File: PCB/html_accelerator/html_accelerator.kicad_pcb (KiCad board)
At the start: 4 copper layers, 129.3 x 104.4 mm, 170 parts, among them J1 Bus_PCI_Express_x16, J2 PCIexpress_bracket, U1 MCS9990, U10 AU6438BS, U11 EMMC_4G, U12 MCS9990, U2 AP1513, U3 CAT24C256YI-GT3, U4 AU6438BS, U5 EMMC_4G, U6 EMMC_4G, U7 EMMC_4G, U8 AU6438BS, U9 AU6438BS, Y1 12MHz, Y2 12MHz, Y3 12MHz, Y4 12MHz, Y5 12MHz

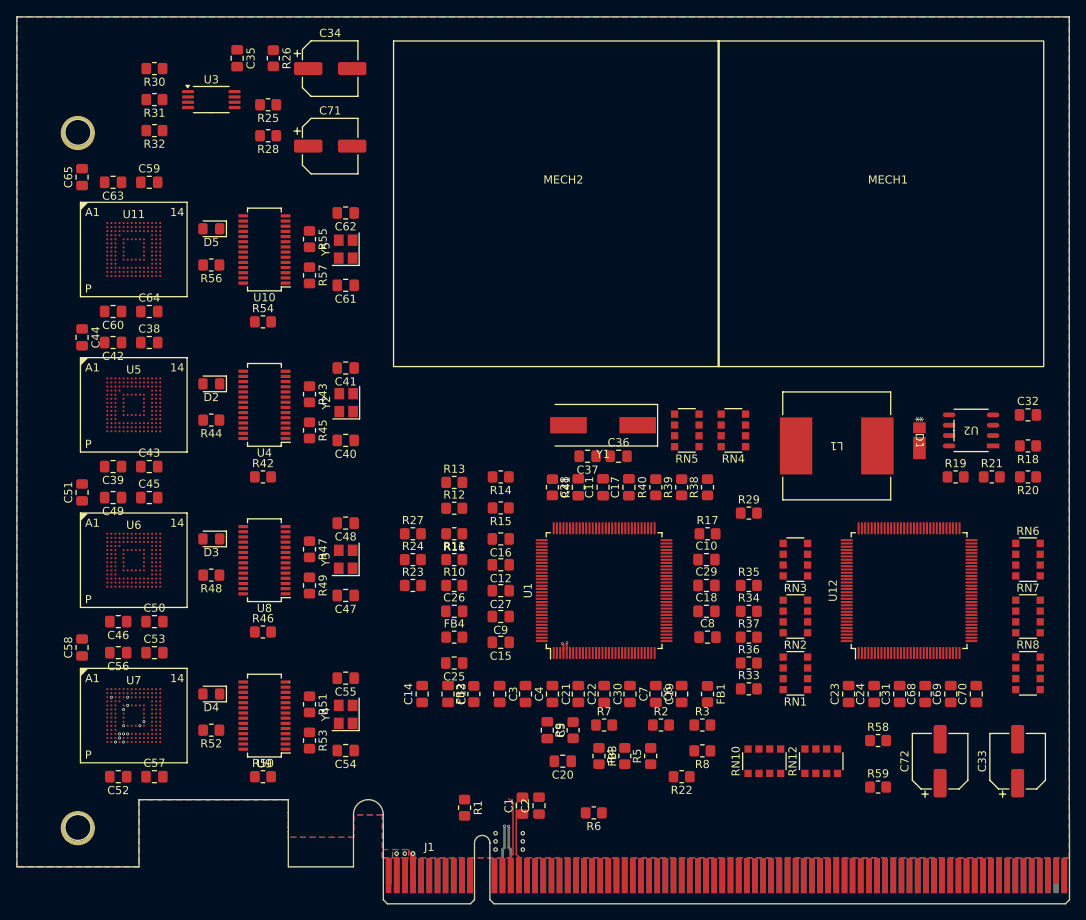
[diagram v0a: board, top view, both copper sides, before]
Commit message: PCIE routing+Shield
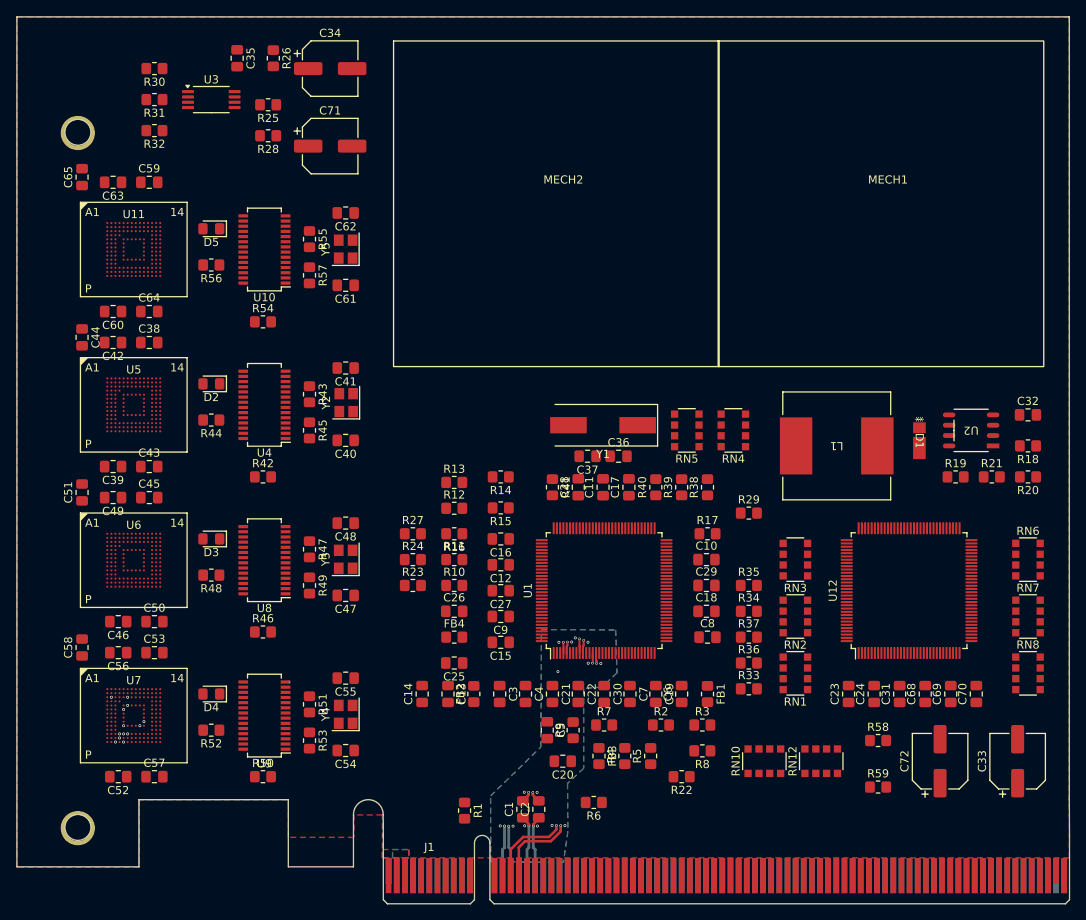
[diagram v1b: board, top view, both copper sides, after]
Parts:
- moved R6 1.28 mm to (185.2, 147.1)
- moved C1 0.45 mm to (176.5, 148.0)
- moved C2 0.45 mm to (178.4, 148.0)
- moved R1 0.35 mm to (169.3, 148.1)
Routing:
- net /PCIE_Slot/85_PCIE_RX_N: track 9.67 -> 42.7 mm, vias 0 -> 2
- net /PCIE_Slot/85_PCIE_RX_P: track 9.69 -> 41.5 mm, vias 0 -> 2
- net /PCIE_Slot/85_PCIE_TXC_P: track 0.00 -> 23.3 mm, vias 0 -> 2
- net /PCIE_Slot/85_PCIE_TXC_N: track 0.00 -> 23.2 mm, vias 0 -> 2
- net /PCIE_Slot/85_PCIE_TX_P: track 0.00 -> 7.55 mm, vias 0 -> 1
- net /PCIE_Slot/85_PCIE_TX_N: track 0.00 -> 7.46 mm, vias 0 -> 1
- net GND: track 2.62 -> 0.00 mm, vias 7 -> 15
- net +12V: track 2.62 -> 0.00 mm, vias 2 -> 0
- net /PCIE_Slot/85_PCIE_CLK_P: track 34.5 -> 36.1 mm
- net /PCIE_Slot/85_PCIE_CLK_N: track 33.2 -> 34.4 mm
- removed copper zone on In2.Cu, net GND

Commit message: trace routing
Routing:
- net +12V: track 0.00 -> 101.1 mm, vias 0 -> 2
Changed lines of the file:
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@@
   )
   (target plus (at 159.467 159.533) (size 5) (width 0.05) (layer "Edge.Cuts"))
+  (segment (start 226.555 146.205) (end 227.755 145.005) (width 1) (layer "F.Cu") (net 4))
+  (segment (start 226.555 149.945) (end 226.555 146.205) (width 1) (layer "F.Cu") (net 4))
+  (segment (start 168.825 144.475) (end 187.095 144.475) (width 1) (layer "F.Cu") (net 4))
+  (segment (start 187.095 144.475) (end 192.565 149.945) (width 1) (layer "F.Cu") (net 4))
+  (segment (start 192.565 149.945) (end 226.555 149.945) (width 1) (layer "F.Cu") (net 4))
+  (segment (start 226.555 149.945) (end 232.525 149.945) (width 1) (layer "F.Cu") (net 4))
+  (segment (start 160.983 153.437) (end 161.025 153.395) (width 0.2) (layer "F.Cu") (net 4))
+  (segment (start 160.983 156.121) (end 160.983 153.437) (width 0.2) (layer "F.Cu") (net 4))
+  (segment (start 237.255 145.215) (end 237.255 144.925) (width 1) (layer "F.Cu") (net 4))
+  (segment (start 161.025 152.275) (end 161.025 152.145) (width 0.2) (layer "F.Cu") (net 4))
+  (segment (start 162.005 153.405) (end 162.005 156.115) (width 0.2) (layer "F.Cu") (net 4))
+  (segment (start 161.025 152.275) (end 168.825 144.475) (width 1) (layer "F.Cu") (net 4))
+  (segment (start 161.025 153.395) (end 161.025 152.275) (width 1) (layer "F.Cu") (net 4))
+  (segment (start 232.525 149.945) (end 237.255 145.215) (width 1) (layer "F.Cu") (net 4))
+  (via (at 161.025 153.395) (size 0.35) (drill 0.2) (layers "F.Cu" "B.Cu") (net 4))
+  (via (at 162.005 153.405) (size 0.35) (drill 0.2) (layers "F.Cu" "B.Cu") (net 4))
+  (segment (start 162.005 153.405) (end 162.005 155.475) (width 0.2) (layer "B.Cu") (net 4))
+  (segment (start 161.025 153.395) (end 161.995 153.395) (width 0.2) (layer "B.Cu") (net 4))
+  (segment (start 161.025 153.395) (end 161.025 155.305) (width 0.2) (layer "B.Cu") (net 4))
+  (segment (start 161.995 153.395) (end 162.005 153.405) (width 0.2) (layer "B.Cu") (net 4))
   (via (at 184.506401 130.015583) (size 0.35) (drill 0.2) (layers "F.Cu" "B.Cu") (free) (net 104))
   (via (at 176.651527 145.863238) (size 0.35) (drill 0.2) (layers "F.Cu" "B.Cu") (free) (net 104))
@@
       )
     )
+  )
+  (zone locked (net 104) (net_name "GND") (layer "B.Cu") (name "PCIE_SHIELD2") (hatch edge 0.5)
+    (priority 3)
+    (connect_pads (clearance 0))
+    (min_thickness 0.25) (filled_areas_thickness no)
+    (fill yes (thermal_gap 0.5) (thermal_bridge_width 0.5))
+    (polygon
+      (pts
+        (xy 181.455 154.485)
+        (xy 172.535 154.395)
+        (xy 172.525 149.555)
+        (xy 182.035 149.555)
+        (xy 182.015 150.655)
+      )
+    )

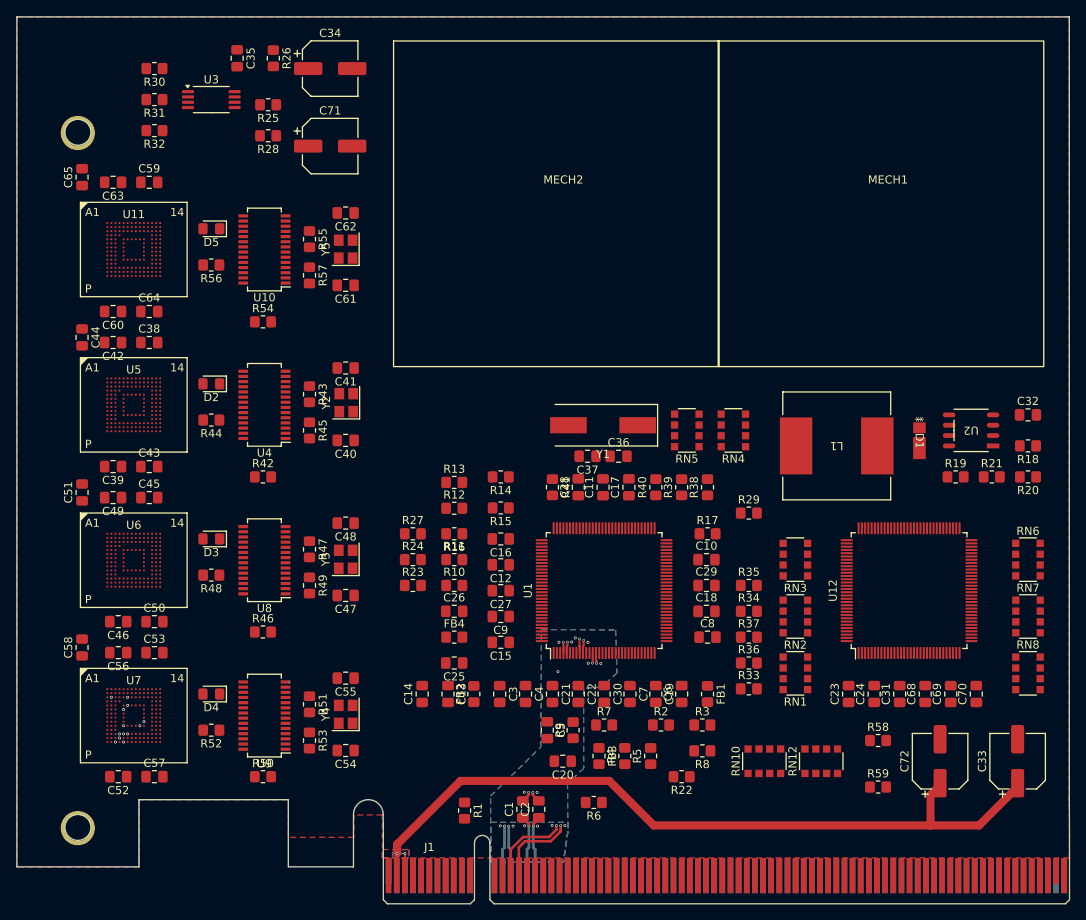
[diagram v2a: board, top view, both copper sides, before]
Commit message: Impedance control routing 90 and 85 ohm
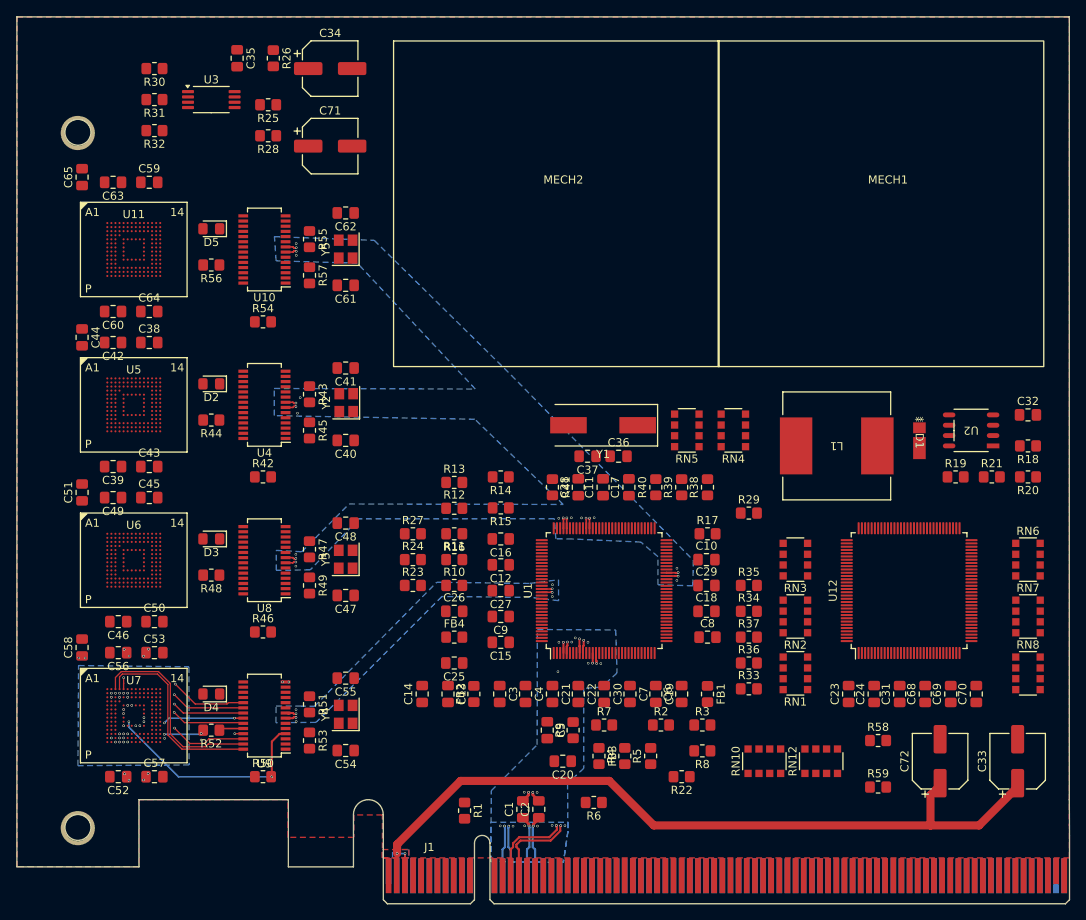
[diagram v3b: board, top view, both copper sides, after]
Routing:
- net 90_USB3_D_N: track 0.00 -> 69.0 mm, vias 0 -> 2
- net 90_USB3_D_P: track 0.00 -> 67.5 mm, vias 0 -> 2
- net 90_USB0_D_N: track 0.00 -> 45.5 mm, vias 0 -> 2
- net 90_USB0_D_P: track 0.00 -> 44.8 mm, vias 0 -> 2
- net 90_USB2_D_N: track 0.00 -> 41.2 mm, vias 0 -> 2
- net 90_USB2_D_P: track 0.00 -> 40.9 mm, vias 0 -> 2
- net 90_USB1_D_N: track 0.00 -> 39.1 mm, vias 0 -> 2
- net 90_USB1_D_P: track 0.00 -> 38.4 mm, vias 0 -> 2
- net Net-(U7A-RST_N): track 0.00 -> 28.1 mm, vias 1 -> 3
- net /eMMC3/DATA_0: track 0.00 -> 25.0 mm
- net /eMMC3/DATA_1: track 0.00 -> 24.3 mm
- net /eMMC3/DATA_3: track 0.00 -> 18.2 mm, vias 0 -> 2
- net /eMMC3/DATA_4: track 0.00 -> 17.7 mm, vias 0 -> 2
- net /eMMC3/DATA_2: track 0.00 -> 17.5 mm, vias 0 -> 2
- net /eMMC3/DATA_5: track 0.00 -> 17.4 mm, vias 0 -> 2
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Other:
- board text added: "ToDo: Route EMMC at 50ohm single end with shield"

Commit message: todolist for routing
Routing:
- net /PCIE_Slot/85_PCIE_RX_P: track 44.1 -> 43.1 mm
- net /PCIE_Slot/85_PCIE_RX_N: track 45.2 -> 44.4 mm
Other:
- board text added: "ToDo: update 85 rounting with new cleaner rules"
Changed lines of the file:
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@@
+    (effects (font (size 1.5 1.5) (thickness 0.3) bold) (justify left bottom))
+  )
+  (gr_text "ToDo:\nupdate 85 rounting with new cleaner rules" (at 164.81 151.53) (layer "Eco2.User")
     (effects (font (size 1.5 1.5) (thickness 0.3) bold) (justify left bottom))
   )
@@
   (segment (start 174.983 156.121) (end 174.983 152.895999) (width 0.2593) (layer "B.Cu") (net 746))
   (segment (start 174.68765 152.600649) (end 174.68765 150.226878) (width 0.2593) (layer "B.Cu") (net 746))
-  (segment (start 174.983 156.121) (end 174.983 152.895999) (width 0.2593) (layer "F.Cu") (net 747))
-  (segment (start 179.72523 151.39535) (end 180.663547 150.457033) (width 0.2593) (layer "F.Cu") (net 747))
-  (segment (start 175.27835 152.141991) (end 176.024991 151.39535) (width 0.2593) (layer "F.Cu") (net 747))
+  (segment (start 174.983 152.895999) (end 175.27835 152.600649) (width 0.2593) (layer "F.Cu") (net 747))
+  (segment (start 175.97523 151.38535) (end 179.70523 151.38535) (width 0.2593) (layer "F.Cu") (net 747))
+  (segment (start 179.70523 151.38535) (end 180.64535 150.44523) (width 0.2593) (layer "F.Cu") (net 747))
+  (segment (start 180.64535 150.44523) (end 180.64535 149.98035) (width 0.2593) (layer "F.Cu") (net 747))
   (segment (start 183.945 127.195) (end 183.945 127.860476) (width 0.2507) (layer "F.Cu") (net 747))
-  (segment (start 176.024991 151.39535) (end 179.72523 151.39535) (width 0.2593) (layer "F.Cu") (net 747))
+  (segment (start 175.27835 152.08223) (end 175.97523 151.38535) (width 0.2593) (layer "F.Cu") (net 747))
   (segment (start 183.945 127.860476) (end 183.85965 127.945826) (width 0.2507) (layer "F.Cu") (net 747))
   (segment (start 183.85965 127.945826) (end 183.85965 128.775) (width 0.2507) (layer "F.Cu") (net 747))
-  (segment (start 180.642846 150.001449) (end 180.596397 149.955) (width 0.2507) (layer "F.Cu") (net 747))
-  (segment (start 180.663547 150.196878) (end 180.640347 150.173678) (width 0.2593) (layer "F.Cu") (net 747))
-  (segment (start 180.640347 149.99895) (end 180.596397 149.955) (width 0.2593) (layer "F.Cu") (net 747))
-  (segment (start 180.663547 150.457033) (end 180.663547 150.196878) (width 0.2593) (layer "F.Cu") (net 747))
-  (segment (start 180.640347 150.173678) (end 180.640347 149.99895) (width 0.2593) (layer "F.Cu") (net 747))
+  (segment (start 174.983 156.121) (end 174.983 152.895999) (width 0.2593) (layer "F.Cu") (net 747))
+  (segment (start 180.64535 149.98035) (end 180.625 149.96) (width 0.2593) (layer "F.Cu") (net 747))
   (segment (start 174.983 156.121) (end 174.983 154.321) (width 0.2593) (layer "F.Cu") (net 747))
-  (segment (start 174.983 152.895999) (end 175.27835 152.600649) (width 0.2593) (layer "F.Cu") (net 747))
-  (segment (start 175.27835 152.600649) (end 175.27835 152.141991) (width 0.2593) (layer "F.Cu") (net 747))
+  (segment (start 175.27835 152.600649) (end 175.27835 152.08223) (width 0.2593) (layer "F.Cu") (net 747))
   (via (at 183.945 127.195) (size 0.3) (drill 0.2) (layers "F.Cu" "B.Cu") (net 747))
-  (via (at 180.596397 149.955) (size 0.3) (drill 0.2) (layers "F.Cu" "B.Cu") (free) (net 747))
+  (via (at 180.625 149.96) (size 0.3) (drill 0.2) (layers "F.Cu" "B.Cu") (net 747))
   (segment (start 186.65465 127.142634) (end 186.65465 130.847366) (width 0.2007) (layer "In2.Cu") (net 747))
-  (segment (start 180.596397 149.955) (end 180.622846 149.928551) (width 0.2507) (layer "In2.Cu") (net 747))
   (segment (start 182.74465 132.417366) (end 182.74465 142.037366) (width 0.2007) (layer "In2.Cu") (net 747))
   (segment (start 186.273328 126.761312) (end 186.65465 127.142634) (width 0.2007) (layer "In2.Cu") (net 747))
@@
   (segment (start 183.117366 132.04465) (end 182.74465 132.417366) (width 0.2007) (layer "In2.Cu") (net 747))
   (segment (start 183.945 127.195) (end 183.945 127.002271) (width 0.2007) (layer "In2.Cu") (net 747))
-  (segment (start 180.672847 144.109169) (end 180.672847 149.87855) (width 0.2007) (layer "In2.Cu") (net 747))
-  (segment (start 180.672847 149.87855) (end 180.596397 149.955) (width 0.2007) (layer "In2.Cu") (net 747))
   (segment (start 186.65465 130.847366) (end 185.457366 132.04465) (width 0.2007) (layer "In2.Cu") (net 747))
+  (segment (start 180.625 149.96) (end 180.60535 149.94035) (width 0.2593) (layer "In2.Cu") (net 747))
   (segment (start 184.185959 126.761312) (end 186.273328 126.761312) (width 0.2007) (layer "In2.Cu") (net 747))
+  (segment (start 180.60535 149.94035) (end 180.60535 144.98) (width 0.2593) (layer "In2.Cu") (net 747))
   (segment (start 185.457366 132.04465) (end 183.117366 132.04465) (width 0.2007) (layer "In2.Cu") (net 747))
   (segment (start 183.945 127.002271) (end 184.185959 126.761312) (width 0.2007) (layer "In2.Cu") (net 747))
-  (segment (start 180.596397 149.965) (end 180.596397 149.955) (width 0.3236) (layer "B.Cu") (net 747))
-  (segment (start 175.68765 152.311531) (end 176.194531 151.80465) (width 0.2593) (layer "F.Cu") (net 748))
+  (segment (start 181.05465 149.98035) (end 181.075 149.96) (width 0.2593) (layer "F.Cu") (net 748))
   (segment (start 183.459762 127.945238) (end 183.459762 128.705) (width 0.2507) (layer "F.Cu") (net 748))
+  (segment (start 175.983 156.121) (end 175.983 152.895999) (width 0.2593) (layer "F.Cu") (net 748))
+  (segment (start 181.05465 150.61477) (end 181.05465 149.98035) (width 0.2593) (layer "F.Cu") (net 748))
+  (segment (start 175.68765 152.25177) (end 176.14477 151.79465) (width 0.2593) (layer "F.Cu") (net 748))
+  (segment (start 176.14477 151.79465) (end 179.87477 151.79465) (width 0.2593) (layer "F.Cu") (net 748))
+  (segment (start 179.87477 151.79465) (end 181.05465 150.61477) (width 0.2593) (layer "F.Cu") (net 748))
   (segment (start 175.983 152.895999) (end 175.68765 152.600649) (width 0.2593) (layer "F.Cu") (net 748))
-  (segment (start 176.194531 151.80465) (end 179.89477 151.80465) (width 0.2593) (layer "F.Cu") (net 748))
-  (segment (start 175.68765 152.600649) (end 175.68765 152.311531) (width 0.2593) (layer "F.Cu") (net 748))
-  (segment (start 179.89477 151.80465) (end 181.072847 150.626573) (width 0.2593) (layer "F.Cu") (net 748))
-  (segment (start 181.072847 150.02215) (end 181.119997 149.975) (width 0.2593) (layer "F.Cu") (net 748))
   (segment (start 183.429649 127.021657) (end 183.429649 127.915125) (width 0.2507) (layer "F.Cu") (net 748))
-  (segment (start 181.093548 150.001449) (end 181.119997 149.975) (width 0.2507) (layer "F.Cu") (net 748))
-  (segment (start 175.983 156.121) (end 175.983 152.895999) (width 0.2593) (layer "F.Cu") (net 748))
-  (segment (start 181.072847 150.626573) (end 181.072847 150.02215) (width 0.2593) (layer "F.Cu") (net 748))
   (segment (start 183.429649 127.915125) (end 183.459762 127.945238) (width 0.2507) (layer "F.Cu") (net 748))
   (segment (start 175.983 156.121) (end 175.983 154.321) (width 0.2593) (layer "F.Cu") (net 748))
-  (via (at 181.119997 149.975) (size 0.3) (drill 0.2) (layers "F.Cu" "B.Cu") (free) (net 748))
+  (segment (start 175.68765 152.600649) (end 175.68765 152.25177) (width 0.2593) (layer "F.Cu") (net 748))
+  (via (at 181.075 149.96) (size 0.3) (drill 0.2) (layers "F.Cu" "B.Cu") (net 748))
   (via (at 183.429649 127.021657) (size 0.3) (drill 0.2) (layers "F.Cu" "B.Cu") (net 748))
   (segment (start 183.09535 142.182634) (end 181.023547 144.254437) (width 0.2007) (layer "In2.Cu") (net 748))
-  (segment (start 181.046747 149.90175) (end 181.119997 149.975) (width 0.2007) (layer "In2.Cu") (net 748))
   (segment (start 185.602634 132.39535) (end 183.262634 132.39535) (width 0.2007) (layer "In2.Cu") (net 748))
-  (segment (start 181.023547 144.254437) (end 181.023547 149.745258) (width 0.2007) (layer "In2.Cu") (net 748))
   (segment (start 187.00535 130.992634) (end 185.602634 132.39535) (width 0.2007) (layer "In2.Cu") (net 748))
-  (segment (start 181.046747 149.768458) (end 181.046747 149.90175) (width 0.2007) (layer "In2.Cu") (net 748))
   (segment (start 183.262634 132.39535) (end 183.09535 132.562634) (width 0.2007) (layer "In2.Cu") (net 748))
-  (segment (start 181.119997 149.975) (end 181.073548 149.928551) (width 0.2507) (layer "In2.Cu") (net 748))
+  (segment (start 181.075 149.96) (end 181.09465 149.94035) (width 0.2593) (layer "In2.Cu") (net 748))
   (segment (start 184.040694 126.410612) (end 186.418596 126.410612) (width 0.2007) (layer "In2.Cu") (net 748))
   (segment (start 183.429649 127.021657) (end 184.040694 126.410612) (width 0.2007) (layer "In2.Cu") (net 748))
   (segment (start 187.00535 126.997366) (end 187.00535 130.992634) (width 0.2007) (layer "In2.Cu") (net 748))
-  (segment (start 181.023547 149.745258) (end 181.046747 149.768458) (width 0.2007) (layer "In2.Cu") (net 748))
+  (segment (start 181.09465 149.94035) (end 181.09465 144.98) (width 0.2593) (layer "In2.Cu") (net 748))
   (segment (start 186.418596 126.410612) (end 187.00535 126.997366) (width 0.2007) (layer "In2.Cu") (net 748))
   (segment (start 183.09535 132.562634) (end 183.09535 142.182634) (width 0.2007) (layer "In2.Cu") (net 748))
-  (segment (start 181.119997 149.965) (end 181.119997 149.975) (width 0.3236) (layer "B.Cu") (net 748))
   (segment (start 186.46 132.7625) (end 186.46 132.53) (width 0.25) (layer "F.Cu") (net 751))
   (segment (start 147.7237 132.3237) (end 147.725 132.325) (width 0.2) (layer "F.Cu") (net 754))
